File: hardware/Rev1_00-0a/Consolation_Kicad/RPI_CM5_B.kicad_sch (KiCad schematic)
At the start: 8 parts, among them J12 RPI_CMx_B

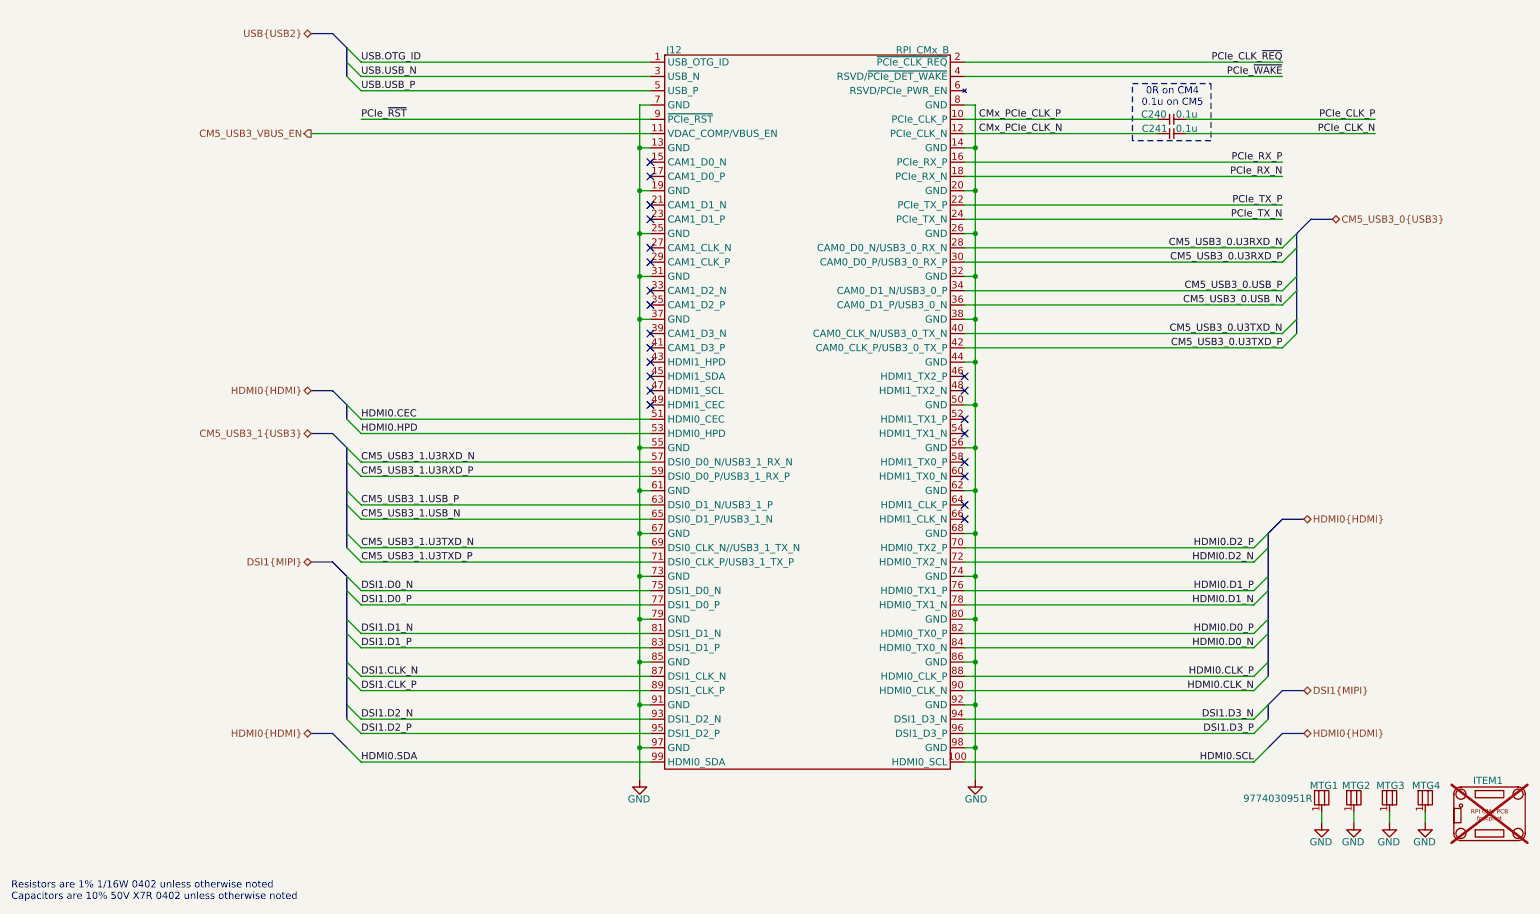
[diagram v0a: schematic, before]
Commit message: Add part number of codec to block diagram Add codec and hdmi schematic sheets
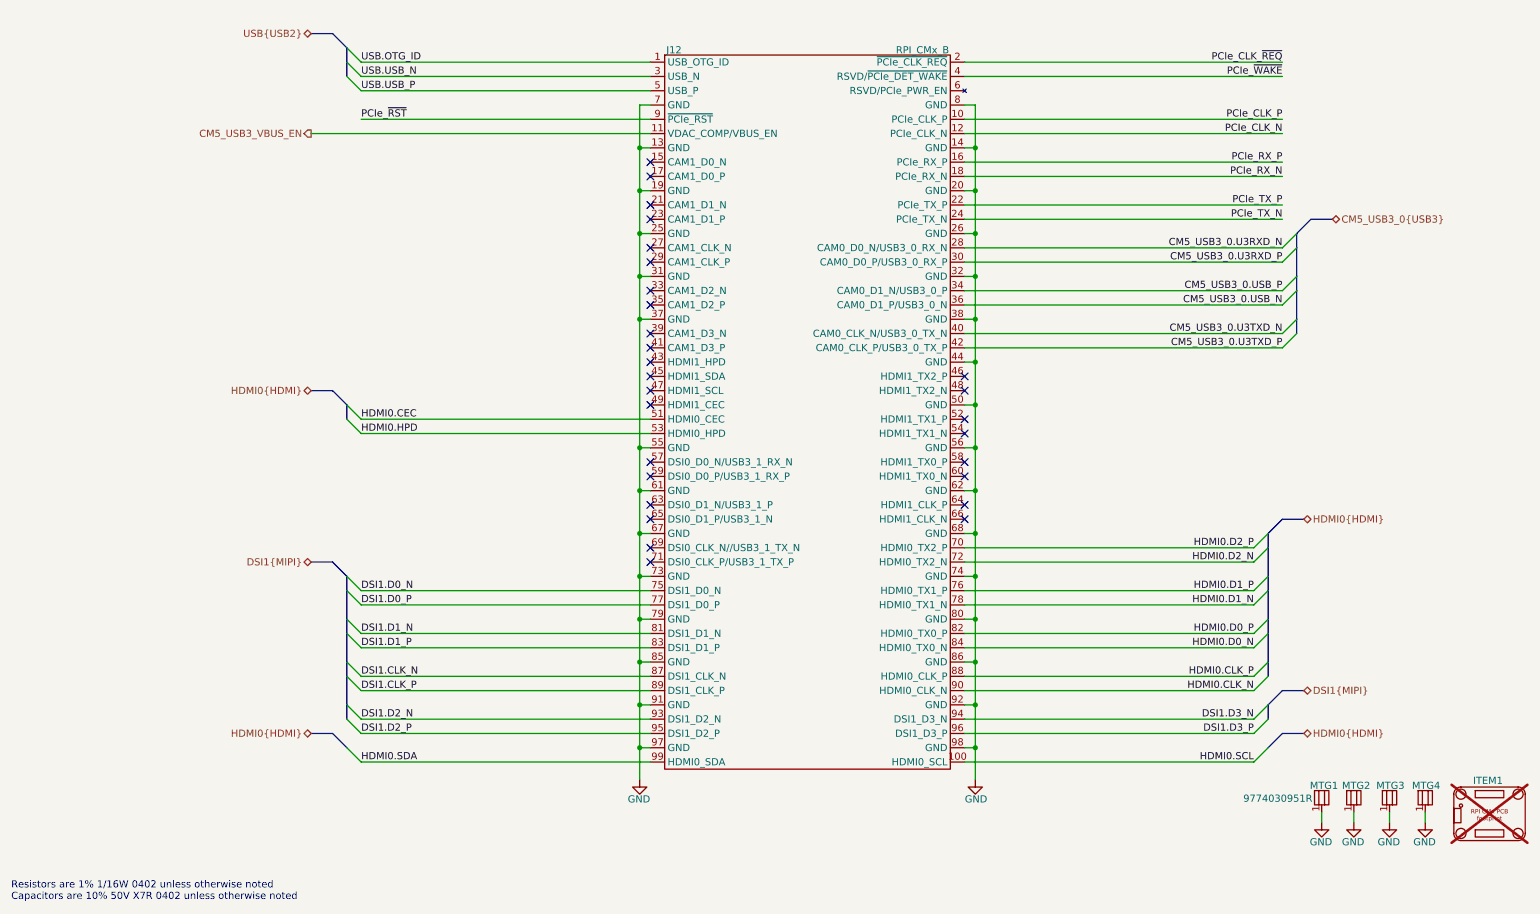
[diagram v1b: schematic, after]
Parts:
- removed C240, C241: 0.1u, footprint:CAP_NONPOL_0402, symbol KicadCompDb:Capacitors/CAP_CER_SMT_00001
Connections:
- net CMx_PCIe_CLK_N is gone; now on net PCIe_CLK_N: J12.12 (PCIe_CLK_N)
- net CMx_PCIe_CLK_P is gone; now on net PCIe_CLK_P: J12.10 (PCIe_CLK_P)
- net CM5_USB3_1.U3RXD_N: no longer names the net of J12.57 (DSI0_D0_N/USB3_1_RX_N)
- net CM5_USB3_1.U3RXD_P: no longer names the net of J12.59 (DSI0_D0_P/USB3_1_RX_P)
- net CM5_USB3_1.U3TXD_N: no longer names the net of J12.69 (DSI0_CLK_N//USB3_1_TX_N)
- net CM5_USB3_1.U3TXD_P: no longer names the net of J12.71 (DSI0_CLK_P/USB3_1_TX_P)
- net CM5_USB3_1.USB_N: no longer names the net of J12.65 (DSI0_D1_P/USB3_1_N)
- net CM5_USB3_1.USB_P: no longer names the net of J12.63 (DSI0_D1_N/USB3_1_P)
- no-connect marks 22 -> 28
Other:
- note removed: "0R on CM4 0.1u on CM5"

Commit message: Update schematics, block diagram and pin mux (good progress G)
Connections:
- net USB2_RP2350.USB_P: now reaches J12.63 (DSI0_D1_N/USB3_1_P)
- net USB2_RP2350.USB_N: now reaches J12.65 (DSI0_D1_P/USB3_1_N)
- net USB.OTG_ID renamed USB2_NATIVE.OTG_ID
- net USB.USB_N renamed USB2_NATIVE.USB_N
- net USB.USB_P renamed USB2_NATIVE.USB_P
- no-connect marks 28 -> 26
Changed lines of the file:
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@@
-	)
-	(no_connect
-		(at 126.365 102.235)
 	)
 	(no_connect
@@
 	)
 	(no_connect
-		(at 126.365 104.775)
-	)
-	(no_connect
 		(at 182.245 89.535)
 	)
@@
 	)
 	(bus_entry
+		(at 72.39 99.695)
+		(size 2.54 2.54)
+		(stroke
+			(width 0)
+			(type default)
+		)
+	)
+	(bus_entry
 		(at 236.22 122.555)
 		(size -2.54 2.54)
@@
 	)
 	(bus_entry
+		(at 72.39 102.235)
+		(size 2.54 2.54)
+		(stroke
+			(width 0)
+			(type default)
+		)
+	)
+	(bus_entry
 		(at 72.39 86.995)
 		(size 2.54 2.54)
@@
 	(wire
 		(pts
+			(xy 126.365 102.235) (xy 74.93 102.235)
+		)
+		(stroke
+			(width 0)
+			(type default)
+		)
+	)
+	(wire
+		(pts
 			(xy 182.245 36.195) (xy 238.76 36.195)
 		)
@@
 		)
 	)
+	(bus
+		(pts
+			(xy 66.04 97.155) (xy 69.85 97.155)
+		)
+		(stroke
+			(width 0)
+			(type default)
+		)
+	)
 	(wire
 		(pts
@@
 	(wire
 		(pts
+			(xy 126.365 104.775) (xy 74.93 104.775)
+		)
+		(stroke
+			(width 0)
+			(type default)
+		)
+	)
+	(wire
+		(pts
 			(xy 74.93 127.635) (xy 126.365 127.635)
 		)
@@
 		)
 	)
+	(bus
+		(pts
+			(xy 69.85 97.155) (xy 72.39 99.695)
+		)
+		(stroke
+			(width 0)
+			(type default)
+		)
+	)
 	(wire
 		(pts
@@
 		(pts
 			(xy 74.93 125.095) (xy 126.365 125.095)
+		)
+		(stroke
+			(width 0)
+			(type default)
+		)
+	)
+	(bus
+		(pts
+			(xy 72.39 99.695) (xy 72.39 102.235)
 		)
 		(stroke
@@
 		)
 	)
-	(label "USB.USB_N"
+	(label "USB2_NATIVE.USB_N"
 		(at 74.93 26.035 0)
 		(effects
@@
 		)
 	)
+	(label "USB2_RP2350.USB_N"
+		(at 74.93 104.775 0)
+		(effects
+			(font
+				(size 1.27 1.27)
+			)
+			(justify left bottom)
+		)
+		(property "Net Class" "DP_90R"
+			(at 104.394 103.886 0)
+			(show_name no)
+			(do_not_autoplace no)
+			(effects
+				(font
+					(size 1.27 1.27)
+					(italic yes)
+				)
+				(justify left)
+			)
+		)
+	)
 	(label "CM5_USB3_0.U3RXD_P"
 		(at 238.76 59.055 180)
@@
 		)
 	)
-	(label "USB.USB_P"
+	(label "USB2_NATIVE.USB_P"
 		(at 74.93 28.575 0)
 		(effects
@@
 		)
 	)
-	(label "USB.OTG_ID"
+	(label "USB2_NATIVE.OTG_ID"
 		(at 74.93 23.495 0)
 		(effects
@@
 		)
 	)
+	(label "USB2_RP2350.USB_P"
+		(at 74.93 102.235 0)
+		(effects
+			(font
+				(size 1.27 1.27)
+			)
+			(justify left bottom)
+		)
+		(property "Net Class" "DP_90R"
+			(at 104.394 101.346 0)
+			(show_name no)
+			(do_not_autoplace no)
+			(effects
+				(font
+					(size 1.27 1.27)
+					(italic yes)
+				)
+				(justify left)
+			)
+		)
+	)
 	(label "CM5_USB3_0.USB_N"
 		(at 238.76 66.675 180)
@@
 				(justify left)
 			)
+		)
+	)
+	(hierarchical_label "USB2_RP2350{USB2}"
+		(shape bidirectional)
+		(at 66.04 97.155 180)
+		(effects
+			(font
+				(size 1.27 1.27)
+			)
+			(justify right)
 		)
 	)
@@
 		)
 	)
-	(hierarchical_label "USB{USB2}"
+	(hierarchical_label "USB2_NATIVE{USB2}"
 		(shape bidirectional)
 		(at 66.04 18.415 180)

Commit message: Work on block diagram and top-level schematic sheet Work on PinMux
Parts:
- added R119, R120: 22R, footprint:RES_0402, symbol KicadCompDb:Resistors/RES_SMT_00015
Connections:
- net CM5_USB3_VBUS_EN: now also R119.2; no longer J12.11 (VDAC_COMP/VBUS_EN)
- new net: J12.11 (VDAC_COMP/VBUS_EN), R119.1, R120.1
- new net RP2350_USB_VBUS: R120.2

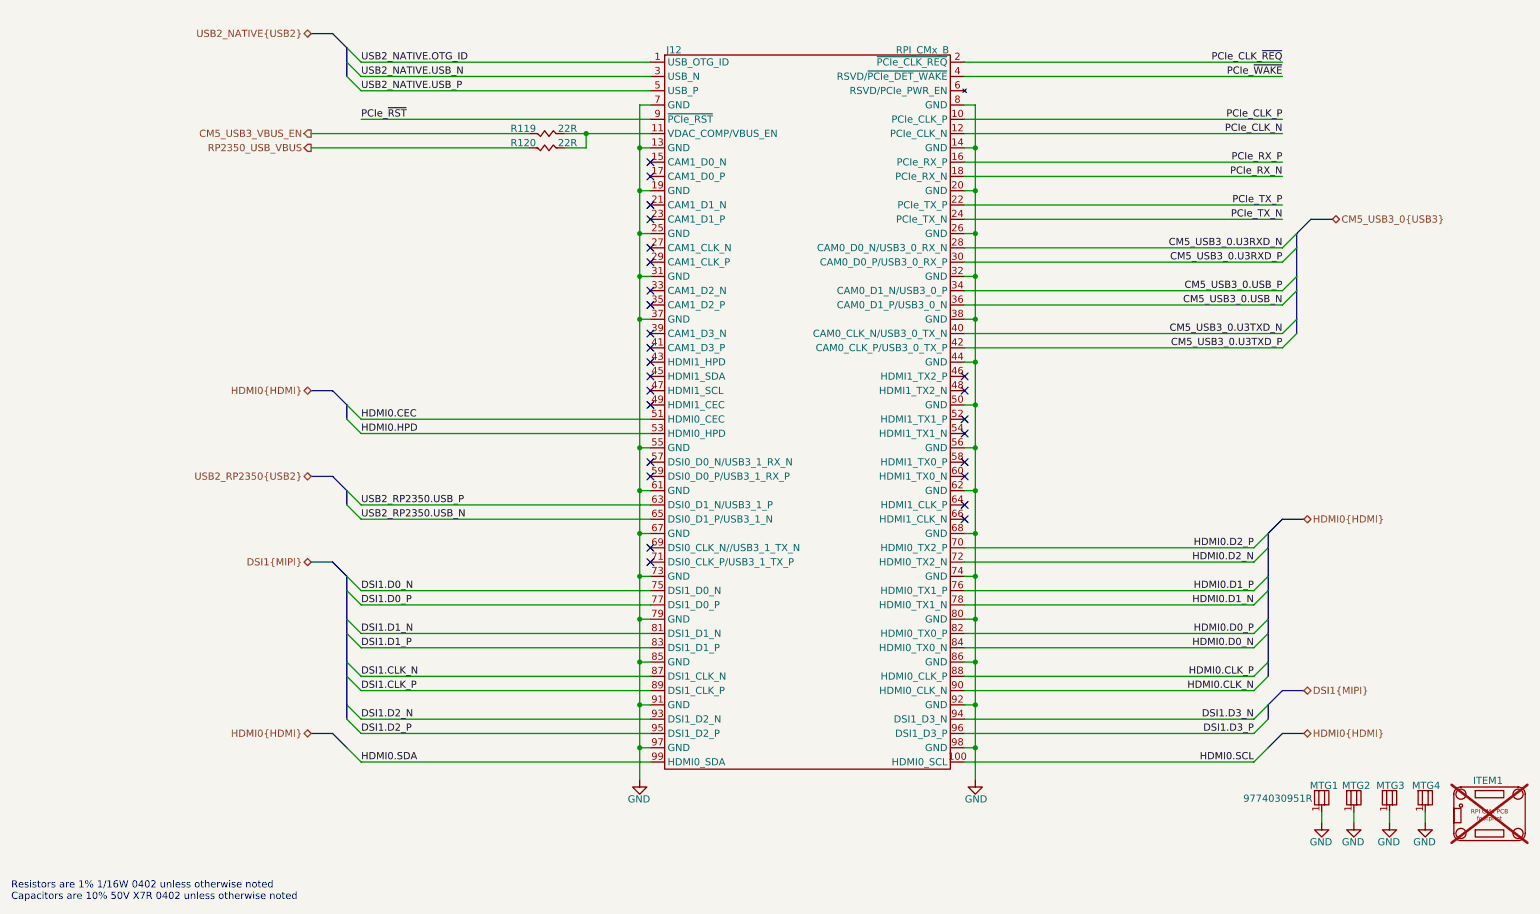
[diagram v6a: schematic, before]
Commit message: Removed unnecessary functions (USB2 mux, CapTouch) Adjusted 220uF alum capacitor for codec (slimmer version)
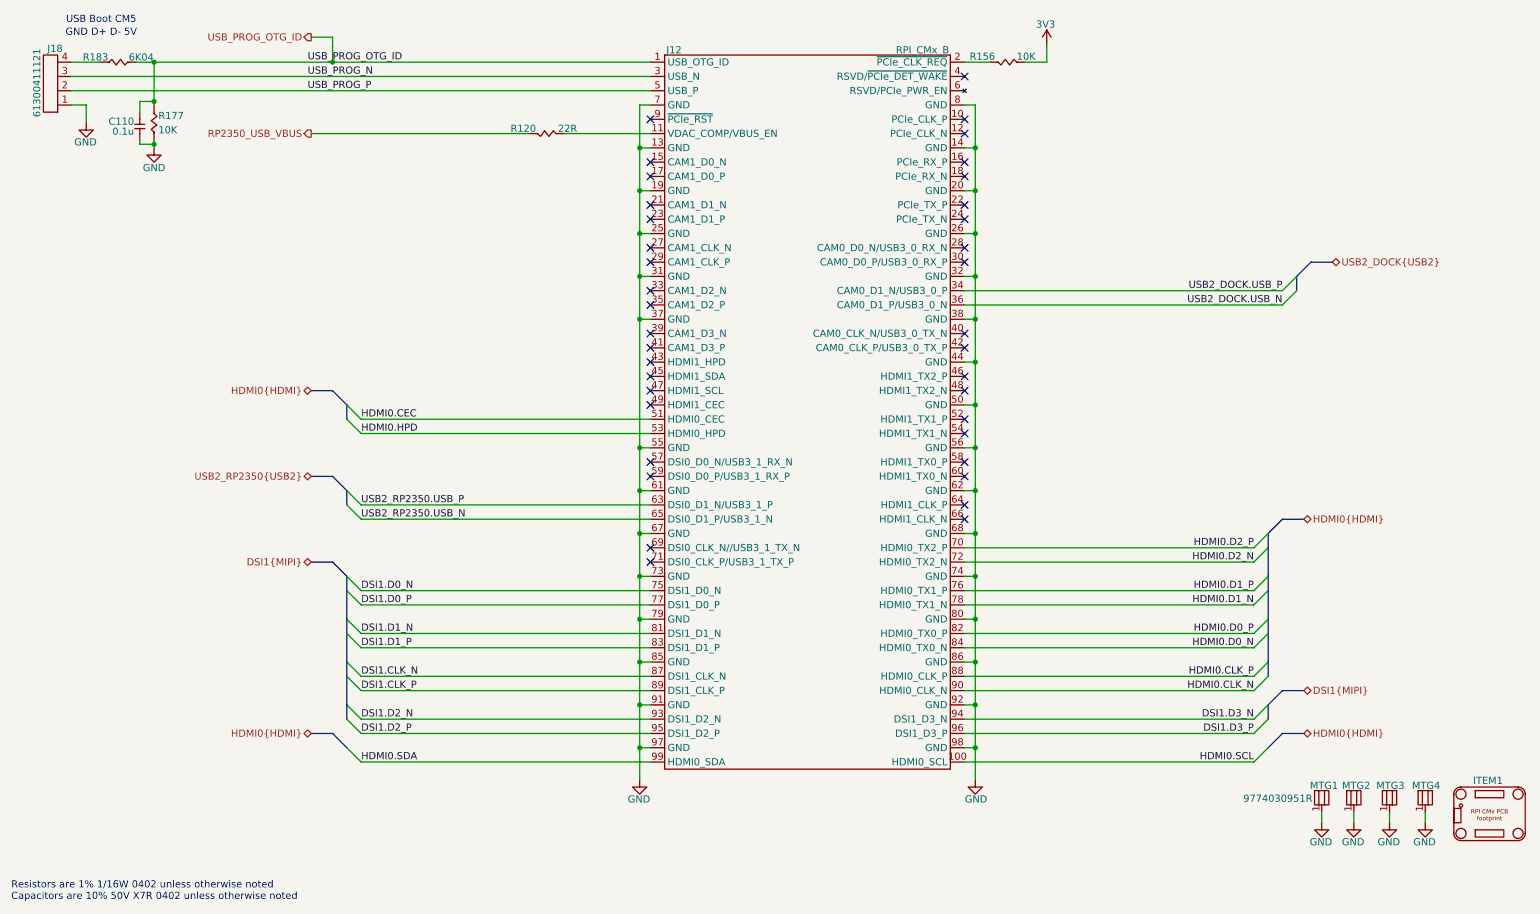
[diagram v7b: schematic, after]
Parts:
- removed R119: 22R, footprint:RES_0402, symbol KicadCompDb:Resistors/RES_SMT_00015
- added C110: 0.1u, footprint:CAP_NONPOL_0402, symbol KicadCompDb:Capacitors/CAP_CER_SMT_00001
- added J18: 61300411121, footprint:HEADER_4P_2_54MM, symbol KicadCompDb:Connector/CONN_00029
- added R156, R177: 10K, footprint:RES_0402, symbol KicadCompDb:Resistors/RES_SMT_00013
- added R183: 6K04, footprint:RES_0402, symbol KicadCompDb:Resistors/RES_SMT_00011
- ITEM1: now fitted
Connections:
- net GND: now also C110.1, J18.1, R177.1
- net CM5_USB3_0.U3RXD_N: no longer names the net of J12.28 (CAM0_D0_N/USB3_0_RX_N)
- net CM5_USB3_0.U3RXD_P: no longer names the net of J12.30 (CAM0_D0_P/USB3_0_RX_P)
- net CM5_USB3_0.U3TXD_N: no longer names the net of J12.40 (CAM0_CLK_N/USB3_0_TX_N)
- net CM5_USB3_0.U3TXD_P: no longer names the net of J12.42 (CAM0_CLK_P/USB3_0_TX_P)
- net CM5_USB3_0.USB_N renamed USB2_DOCK.USB_N
- net CM5_USB3_0.USB_P renamed USB2_DOCK.USB_P
- net PCIe_CLK_N: no longer names the net of J12.12 (PCIe_CLK_N)
- net PCIe_CLK_P: no longer names the net of J12.10 (PCIe_CLK_P)
- net PCIe_CLK_~{REQ}: no longer names the net of J12.2 (~{PCIe_CLK_REQ})
- net PCIe_CLK_~{REQ}: now also R156.2
- net PCIe_RX_N: no longer names the net of J12.18 (PCIe_RX_N)
- net PCIe_RX_P: no longer names the net of J12.16 (PCIe_RX_P)
- net PCIe_TX_N: no longer names the net of J12.24 (PCIe_TX_N)
- net PCIe_TX_P: no longer names the net of J12.22 (PCIe_TX_P)
- net PCIe_~{RST}: no longer names the net of J12.9 (~{PCIe_RST})
- net PCIe_~{WAKE}: no longer names the net of J12.4 (RSVD/~{PCIe_DET_WAKE})
- net USB2_NATIVE.OTG_ID renamed USB_PROG_OTG_ID
- net USB_PROG_OTG_ID: now also C110.2, R177.2, R183.1
- net USB2_NATIVE.USB_N renamed USB_PROG_N
- net USB_PROG_N: now also J18.3
- net USB2_NATIVE.USB_P renamed USB_PROG_P
- net USB_PROG_P: now also J18.2
- new net: J18.4, R183.2
- new net 3V3: R156.1
- no-connect marks 26 -> 38
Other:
- note added: "GND D+ D- 5V"
- note added: "USB Boot CM5"
- moved on the sheet: R120

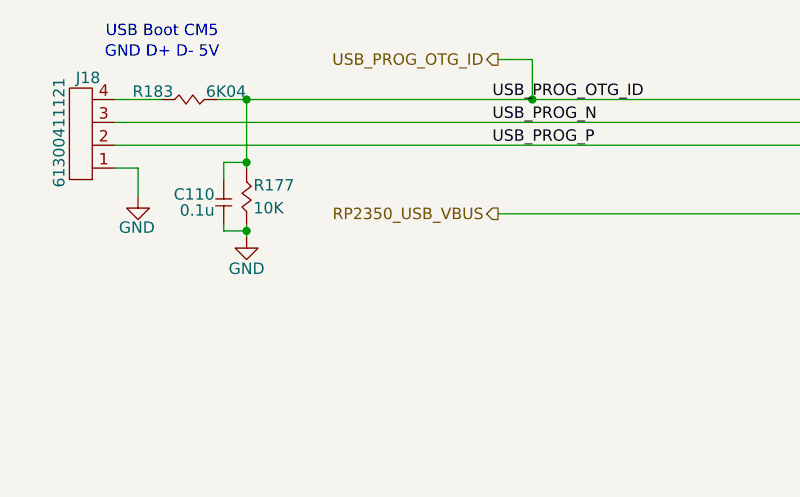
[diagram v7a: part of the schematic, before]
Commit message: Work on preliminary placement + RP2350A fanout
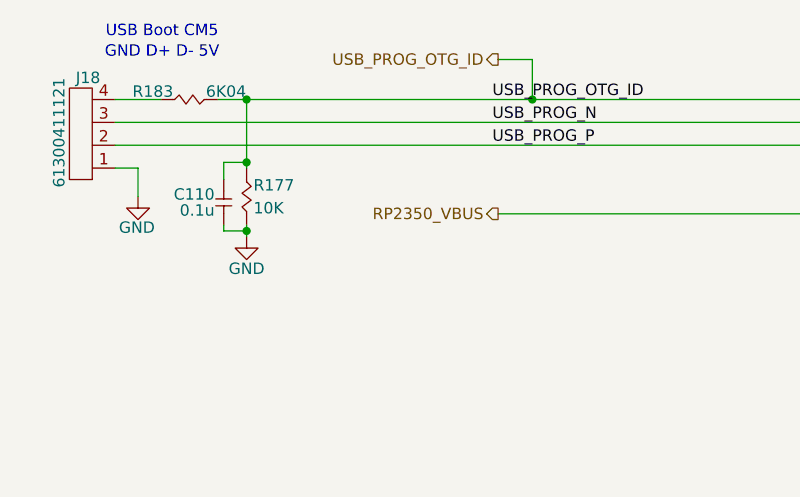
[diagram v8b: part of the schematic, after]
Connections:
- net RP2350_USB_VBUS renamed RP2350_VBUS
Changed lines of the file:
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@@
 		)
 	)
-	(hierarchical_label "RP2350_USB_VBUS"
+	(hierarchical_label "RP2350_VBUS"
 		(shape output)
 		(at 66.04 36.195 180)
